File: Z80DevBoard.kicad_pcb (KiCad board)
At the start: 2 copper layers, 219 x 107.5 mm, 143 parts, among them SW1 WAIT, SW2 RESET, SW3 Z80BOOT, SW4 RPBOOT

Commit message: Added the values of the resistors and of the condensators.
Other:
- board text added: "0"
- board text added: "0.1uF"
- board text added: "10k"
- board text added: "10uF"
- board text added: "1uF"
- board text added: "220"
- board text added: "5k"

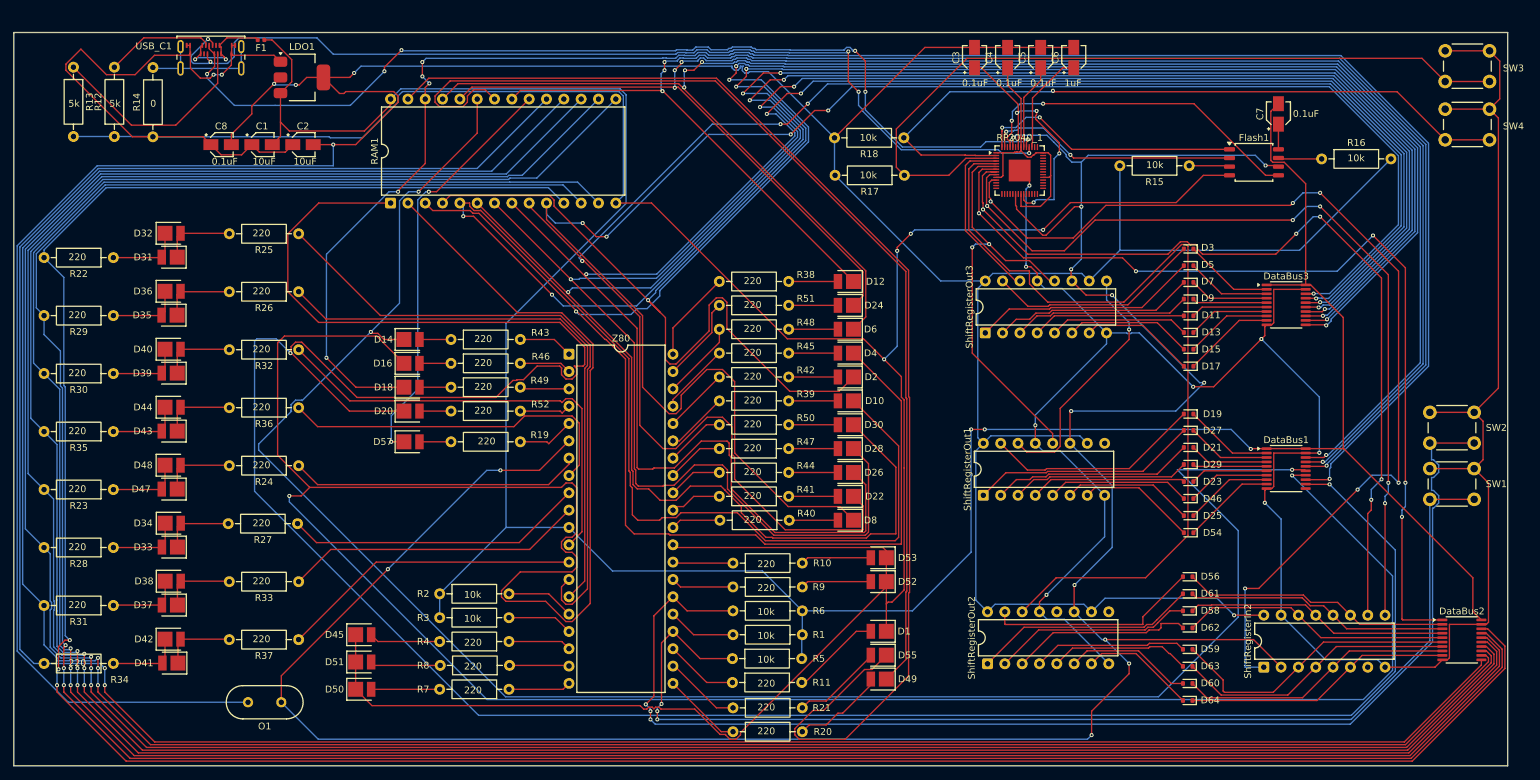
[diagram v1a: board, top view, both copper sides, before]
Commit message: Added the buttons names. Fixed some texts. Updated the gerber files.
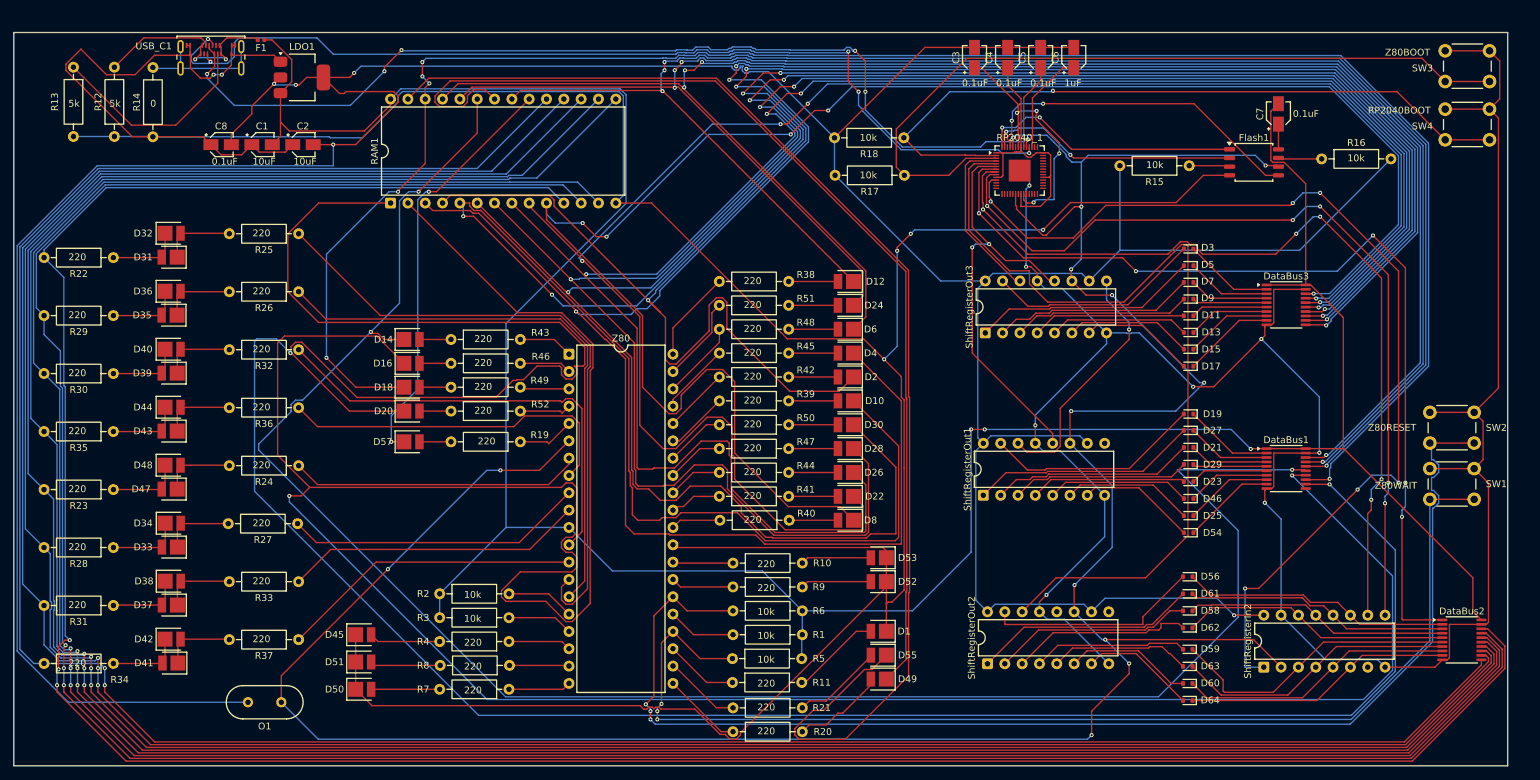
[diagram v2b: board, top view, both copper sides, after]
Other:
- board text added: "RP2040BOOT"
- board text added: "Z80BOOT"
- board text added: "Z80RESET"
- board text added: "Z80WAIT"
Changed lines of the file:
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@@
 		(tags "tact sw push 6mm")
 		(property "Reference" "SW3"
-			(at 10 2.55 0)
+			(at -3.33395 2.55 0)
 			(layer "F.SilkS")
 			(effects
@@
 		)
 		(property "Value" "Z80BOOT"
-			(at -5.5 2.55 0)
+			(at -5.33395 0.316 0)
 			(layer "F.Fab")
 			(effects
@@
 		(tags "Resistor Axial_DIN0207 series Axial Horizontal pin pitch 10.16mm 0.25W = 1/4W length 6.3mm diameter 2.5mm")
 		(property "Reference" "R13"
-			(at 5.08 -2.37 90)
+			(at 5.08 2.7415 90)
 			(layer "F.SilkS")
 			(effects
@@
 		(tags "tact sw push 6mm")
 		(property "Reference" "SW4"
-			(at 10 2.5 0)
+			(at -3.33395 2.5 0)
 			(layer "F.SilkS")
 			(effects
@@
 		)
 		(property "Value" "RPBOOT"
-			(at -5 2.5 0)
+			(at -4.83395 0.266 0)
 			(layer "F.Fab")
 			(effects
@@
 		)
 	)
+	(gr_text "Z80WAIT"
+		(at 237.5 105.5 0)
+		(layer "F.SilkS")
+		(effects
+			(font
+				(size 1 1)
+				(thickness 0.15)
+			)
+			(justify left bottom)
+		)
+	)
 	(gr_text "220"
 		(at 145 82.5 0)
@@
 		)
 	)
+	(gr_text "Z80RESET"
+		(at 236.5 97 0)
+		(layer "F.SilkS")
+		(effects
+			(font
+				(size 1 1)
+				(thickness 0.15)
+			)
+			(justify left bottom)
+		)
+	)
 	(gr_text "220"
 		(at 46 131.5 0)
@@
 		)
 	)
+	(gr_text "RP2040BOOT"
+		(at 236.5 50.5 0)
+		(layer "F.SilkS")
+		(effects
+			(font
+				(size 1 1)
+				(thickness 0.15)
+			)
+			(justify left bottom)
+		)
+	)
 	(gr_text "10k"
 		(at 104 125 0)
@@
 		(layer "F.SilkS")
 		(effects
+			(font
+				(size 1 1)
+				(thickness 0.15)
+			)
+			(justify left bottom)
+		)
+	)
+	(gr_text "Z80BOOT"
+		(at 239 42 0)
+		(layer "F.SilkS")
+		(effects

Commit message: Added the info about the author and the github.
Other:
- board text added: "Z80DevBoard Author: Gianluca Rainis GitHub: gianluca-rainis Repo: https://github.com/gianluca-rainis/Z80DevBoard"
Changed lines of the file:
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@@
+		)
+	)
+	(gr_text "Z80DevBoard\n\nAuthor: Gianluca Rainis\nGitHub: gianluca-rainis\nRepo: https://github.com/gianluca-rainis/Z80DevBoard"
+		(at 82.5 145 0)
+		(layer "B.SilkS")
+		(effects
+			(font
+				(size 1 1)
+				(thickness 0.2)
+				(bold yes)
+			)
+			(justify left bottom mirror)
 		)
 	)

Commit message: Added the graphics in the back. Updated the gerber files.
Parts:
- added G***: LOGO, LOGO, B.Cu at (251.5, 143.5)
- added G***: LOGO, LOGO, B.Cu at (190.1, 63.8)

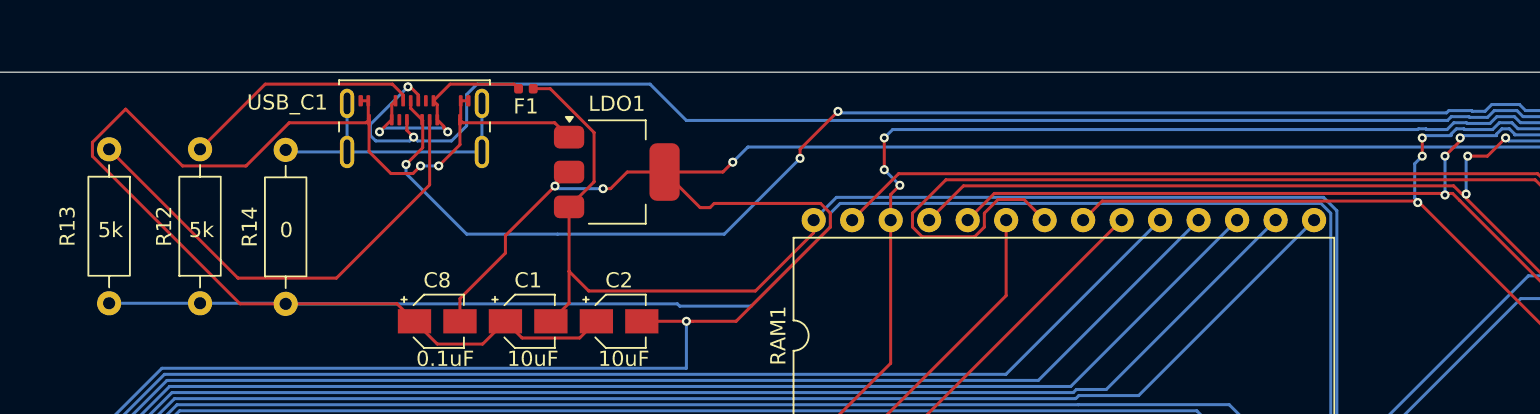
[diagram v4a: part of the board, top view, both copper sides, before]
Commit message: Updated the USB C port.
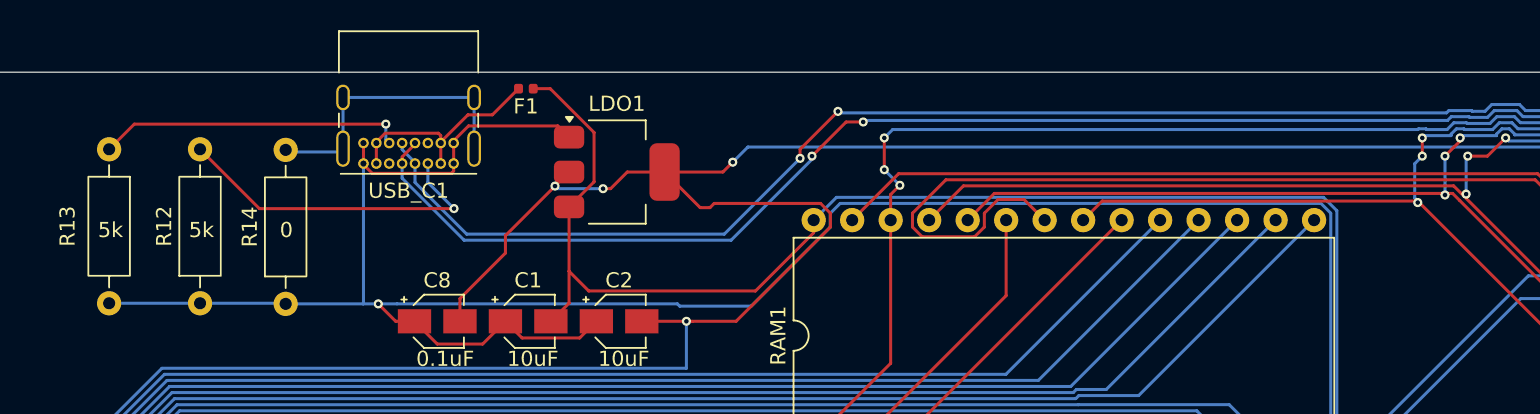
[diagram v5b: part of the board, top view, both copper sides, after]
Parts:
- USB_C1: footprint Connector_USB:USB_C_Receptacle_Amphenol_124019772112A -> Connector_USB:USB_C_Receptacle_GCT_USB4085
- moved USB_C1 2.75 mm to (69.5, 44.5), turned to 180 degrees
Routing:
- net GND: track 835.1 -> 794.2 mm, vias 14 -> 13
- net USB-C-CC2: track 31.5 -> 20.3 mm, vias 0 -> 1
- net USB-C-CC1: track 15.9 -> 22.1 mm, vias 0 -> 1
- net USB-RP2040-DM: track 145.7 -> 140.4 mm
- net USB-RP2040-DP: track 144.3 -> 140.8 mm, vias 6 -> 5
- net USB-C-VBUS: track 15.8 -> 14.5 mm, vias 2 -> 0

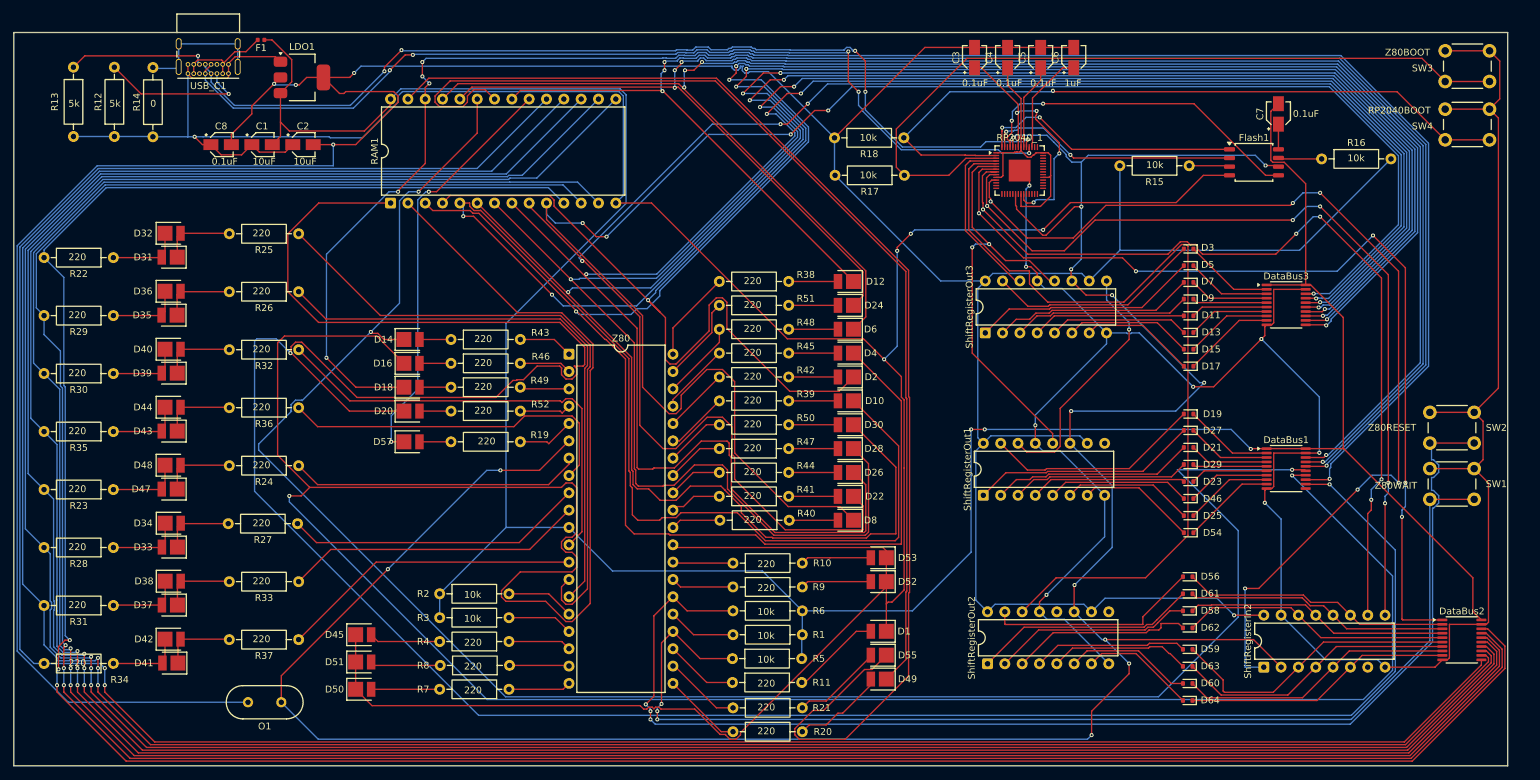
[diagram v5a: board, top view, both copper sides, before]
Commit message: Fixed the borders of the board.
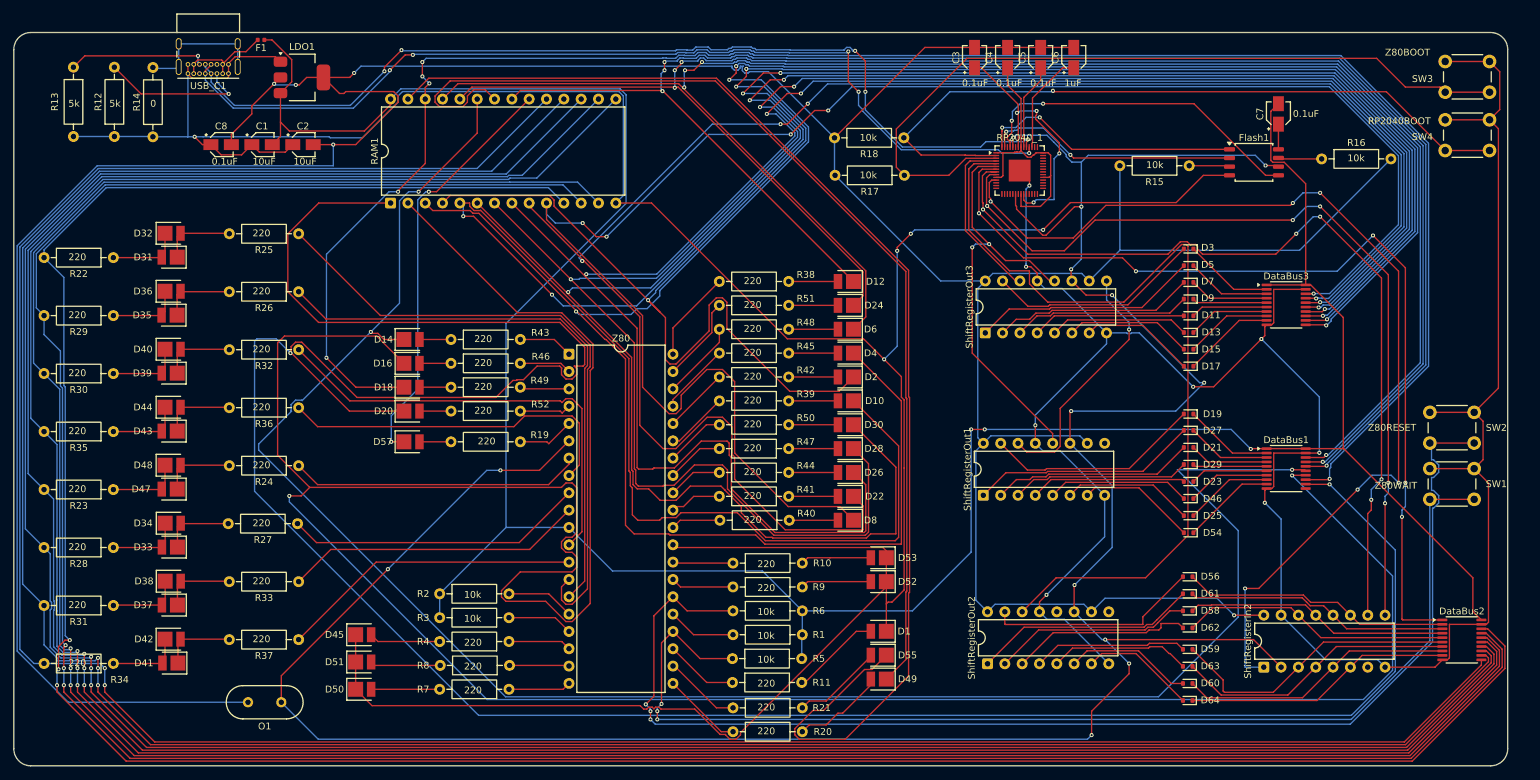
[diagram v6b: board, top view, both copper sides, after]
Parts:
- moved SW3 1.57 mm to (247.8, 42.8)
- moved SW4 1.57 mm to (247.8, 51.3)
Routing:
- net GND: track 794.2 -> 792.6 mm
- net RP2040-Z80BOOTMODE: track 114.4 -> 115.1 mm
- net RP2040-RPBOOTMODE: track 106.3 -> 107.0 mm
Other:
- outline, holes or cut-outs redrawn
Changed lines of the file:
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@@
 	(title_block
 		(title "Z80DevBoard")
-		(date "2025-12-15")
+		(date "2025-12-16")
 		(company "Gianluca Rainis")
 		(comment 1 "gianluca-rainis on GitHub")
@@
 	(footprint "Button_Switch_THT:SW_PUSH_6mm_H7.3mm"
 		(layer "F.Cu")
-		(at 247.83395 41.184)
+		(at 247.83395 42.75)
 		(descr "tactile push button, 6x6mm e.g. PHAP33xx series, height=7.3mm")
 		(tags "tact sw push 6mm")
@@
 	(footprint "Button_Switch_THT:SW_PUSH_6mm_H7.3mm"
 		(layer "F.Cu")
-		(at 247.83395 49.734)
+		(at 247.83395 51.3)
 		(descr "tactile push button, 6x6mm e.g. PHAP33xx series, height=7.3mm")
 		(tags "tact sw push 6mm")
@@
 		(embedded_fonts no)
 	)
-	(gr_rect
-		(start 38 38.5)
-		(end 257 146)
+	(gr_line
+		(start 257 41)
+		(end 257 143.5)
+		(stroke
+			(width 0.05)
+			(type default)
+		)
+		(layer "Edge.Cuts")
+	)
+	(gr_arc
+		(start 38 41)
+		(mid 38.732233 39.232233)
+		(end 40.5 38.5)
+		(stroke
+			(width 0.05)
+			(type default)
+		)
+		(layer "Edge.Cuts")
+	)
+	(gr_arc
+		(start 257 143.5)
+		(mid 256.267767 145.267767)
+		(end 254.5 146)
+		(stroke
+			(width 0.05)
+			(type default)
+		)
+		(layer "Edge.Cuts")
+	)
+	(gr_line
+		(start 38 143.5)
+		(end 38 41)
+		(stroke
+			(width 0.05)
+			(type default)
+		)
+		(layer "Edge.Cuts")
+	)
+	(gr_line
+		(start 254.5 146)
+		(end 40.5 146)
+		(stroke
+			(width 0.05)
+			(type default)
+		)
+		(layer "Edge.Cuts")
+	)
+	(gr_arc
+		(start 254.5 38.5)
+		(mid 256.267767 39.232233)
+		(end 257 41)
+		(stroke
+			(width 0.05)
+			(type default)
+		)
+		(layer "Edge.Cuts")
+	)
+	(gr_line
+		(start 40.5 38.5)
+		(end 254.5 38.5)
+		(stroke
+			(width 0.05)
+			(type default)
+		)
+		(layer "Edge.Cuts")
+	)
+	(gr_arc
+		(start 40.5 146)
+		(mid 38.732233 145.267767)
+		(end 38 143.5)
 		(stroke
 			(width 0.05)
 			(type default)
 		)
-		(fill no)
 		(layer "Edge.Cuts")
 	)
@@
 	)
 	(gr_text "RP2040BOOT"
-		(at 236.5 50.5 0)
+		(at 236.5 52.066 0)
 		(layer "F.SilkS")
 		(effects
@@
 	)
 	(segment
+		(start 252.08395 94.184)
+		(end 255.63495 90.633)
+		(width 0.2)
+		(layer "F.Cu")
+		(net 20)
+	)
+	(segment
 		(start 90.5105 137.184)
 		(end 88.1095 134.783)
@@
 	)
 	(segment
-		(start 254.33395 49.734)
-		(end 247.83395 49.734)
+		(start 254.33395 51.3)
+		(end 247.83395 51.3)
 		(width 0.2)
 		(layer "F.Cu")
@@
 	)
 	(segment
-		(start 254.33395 41.184)
-		(end 247.83395 41.184)
+		(start 254.33395 42.75)
+		(end 247.83395 42.75)
 		(width 0.2)
 		(layer "F.Cu")
@@
 	)
 	(segment
+		(start 255.63495 52.601)
+		(end 254.33395 51.3)
+		(width 0.2)
+		(layer "F.Cu")
+		(net 20)
+	)
+	(segment
 		(start 64.105346 45.176)
 		(end 63.525 44.595654)
@@
 	)
 	(segment
-		(start 255.83395 42.684)
-		(end 255.83395 48.234)
+		(start 255.83395 44.25)
+		(end 255.83395 49.8)
 		(width 0.2)
 		(layer "F.Cu")
@@
 	)
 	(segment
-		(start 255.63495 90.633)
-		(end 252.08395 94.184)
-		(width 0.2)
-		(layer "F.Cu")
-		(net 20)
-	)
-	(segment
 		(start 69.318974 45.176)
 		(end 64.105346 45.176)
@@
 	)
 	(segment
-		(start 254.33395 49.734)
-		(end 255.63495 51.035)
-		(width 0.2)
-		(layer "F.Cu")
-		(net 20)
-	)
-	(segment
 		(start 137.8284 137.684)
 		(end 132.866893 137.684)
@@
 	)
 	(segment
-		(start 254.33395 41.184)
-		(end 255.83395 42.684)
+		(start 254.33395 42.75)
+		(end 255.83395 44.25)
 		(width 0.2)
 		(layer "F.Cu")
@@
 	)
 	(segment
-		(start 255.63495 51.035)
-		(end 255.63495 90.633)
+		(start 255.63495 90.633)
+		(end 255.63495 52.601)
 		(width 0.2)
 		(layer "F.Cu")
@@
 	)
 	(segment
-		(start 255.83395 48.234)
-		(end 254.33395 49.734)
+		(start 255.83395 49.8)
+		(end 254.33395 51.3)
 		(width 0.2)
 		(layer "F.Cu")
@@
 	)
 	(segment
+		(start 167.3705 58.255)
+		(end 168.5515 59.436)
+		(width 0.2)
+		(layer "F.Cu")
+		(net 172)
+	)
+	(segment
 		(start 167.3705 52.64545)
 		(end 167.3705 58.255)
@@
 	)
 	(segment
-		(start 247.83395 45.684)
-		(end 244.43295 42.283)
+		(start 247.83395 47.25)
+		(end 247.08395 46.5)
 		(width 0.2)
 		(layer "F.Cu")
@@
 	)
 	(segment
-		(start 175.064 59.436)
-		(end 168.5515 59.436)
+		(start 247.08395 46.5)
+		(end 242 46.5)
 		(width 0.2)
 		(layer "F.Cu")
@@
 	)
 	(segment
-		(start 182.0165 56.936)
-		(end 177.564 56.936)
+		(start 175.064 59.436)
+		(end 168.5515 59.436)
 		(width 0.2)
 		(layer "F.Cu")
@@
 	)
 	(segment
-		(start 244.43295 42.283)
-		(end 177.73295 42.283)
+		(start 242 46.5)
+		(end 237.783 42.283)
 		(width 0.2)
 		(layer "F.Cu")
@@
 	)
 	(segment
-		(start 254.33395 45.684)
-		(end 247.83395 45.684)
+		(start 182.0165 56.936)
+		(end 177.564 56.936)
 		(width 0.2)
 		(layer "F.Cu")
@@
 	)
 	(segment
-		(start 167.3705 58.255)
-		(end 168.5515 59.436)
+		(start 254.33395 47.25)
+		(end 247.83395 47.25)
 		(width 0.2)
 		(layer "F.Cu")
@@
 	)
 	(segment
+		(start 237.783 42.283)
+		(end 177.73295 42.283)
+		(width 0.2)
+		(layer "F.Cu")
+		(net 172)
+	)
+	(segment
 		(start 168.4715 53.936)
 		(end 171 56.4645)
@@
 	)
 	(segment
-		(start 177.4645 56.4645)
-		(end 177.5 56.5)
+		(start 190.47695 47.184)
+		(end 239.21795 47.184)
 		(width 0.2)
 		(layer "F.Cu")
@@
 	)
 	(segment
-		(start 178.964 56.536)
-		(end 182.0165 56.536)
+		(start 177.4645 56.4645)
+		(end 177.5 56.5)
 		(width 0.2)
 		(layer "F.Cu")
@@
 	)
 	(segment
-		(start 190.47695 47.184)
-		(end 240.78395 47.184)
+		(start 178.964 56.536)
+		(end 182.0165 56.536)
 		(width 0.2)
 		(layer "F.Cu")
@@
 	)
 	(segment
-		(start 254.33395 54.234)
-		(end 247.83395 54.234)
+		(start 254.33395 55.8)
+		(end 247.83395 55.8)
 		(width 0.2)
 		(layer "F.Cu")
@@
 	)
 	(segment
-		(start 178.928 56.5)
-		(end 178.964 56.536)
+		(start 239.21795 47.184)
+		(end 247.83395 55.8)
 		(width 0.2)
 		(layer "F.Cu")
@@
 	)
 	(segment
-		(start 240.78395 47.184)
-		(end 247.83395 54.234)
+		(start 178.928 56.5)
+		(end 178.964 56.536)
 		(width 0.2)
 		(layer "F.Cu")
